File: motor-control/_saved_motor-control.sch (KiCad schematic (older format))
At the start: 8 parts

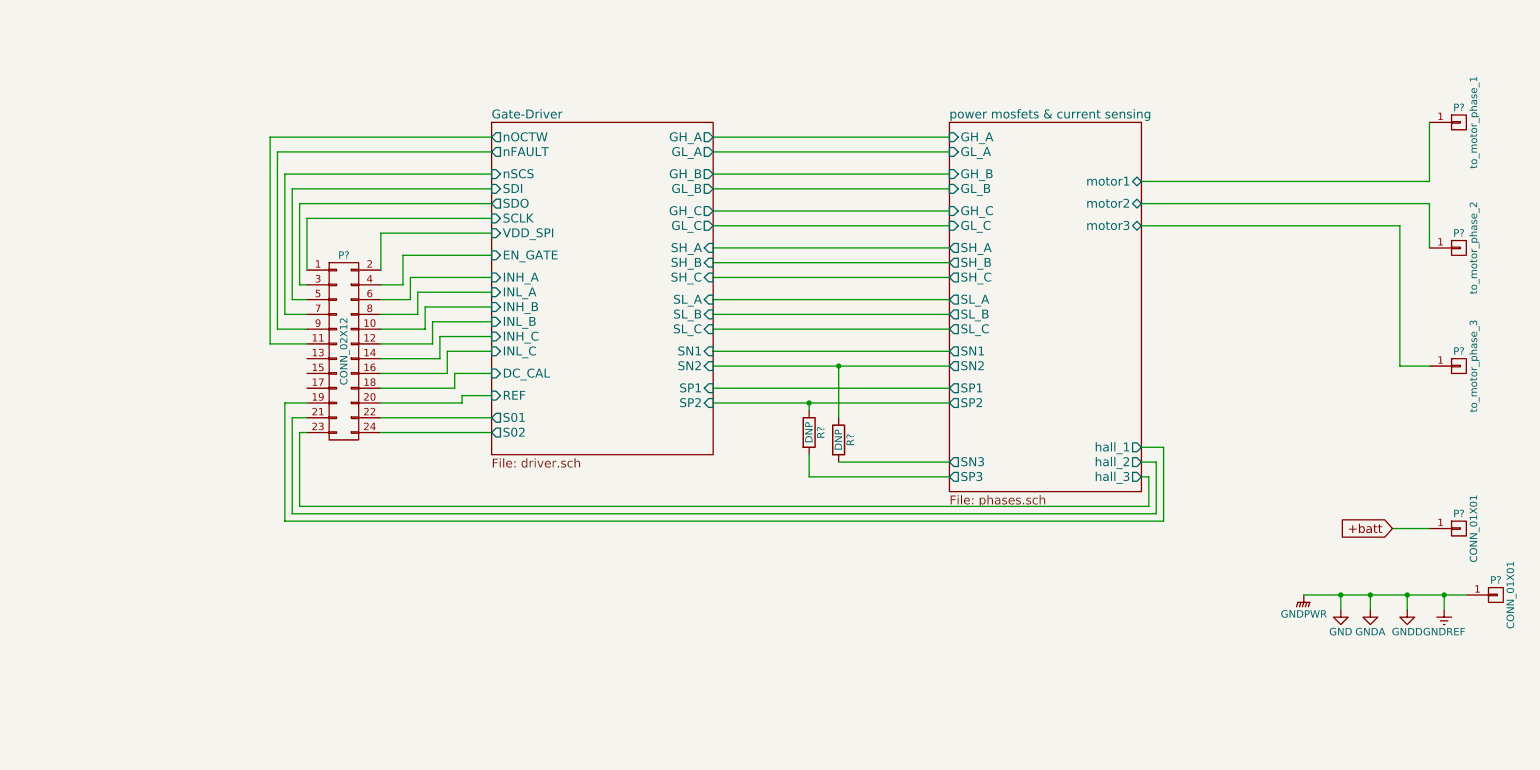
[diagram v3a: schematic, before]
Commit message: Annotated schematic & matched footprints
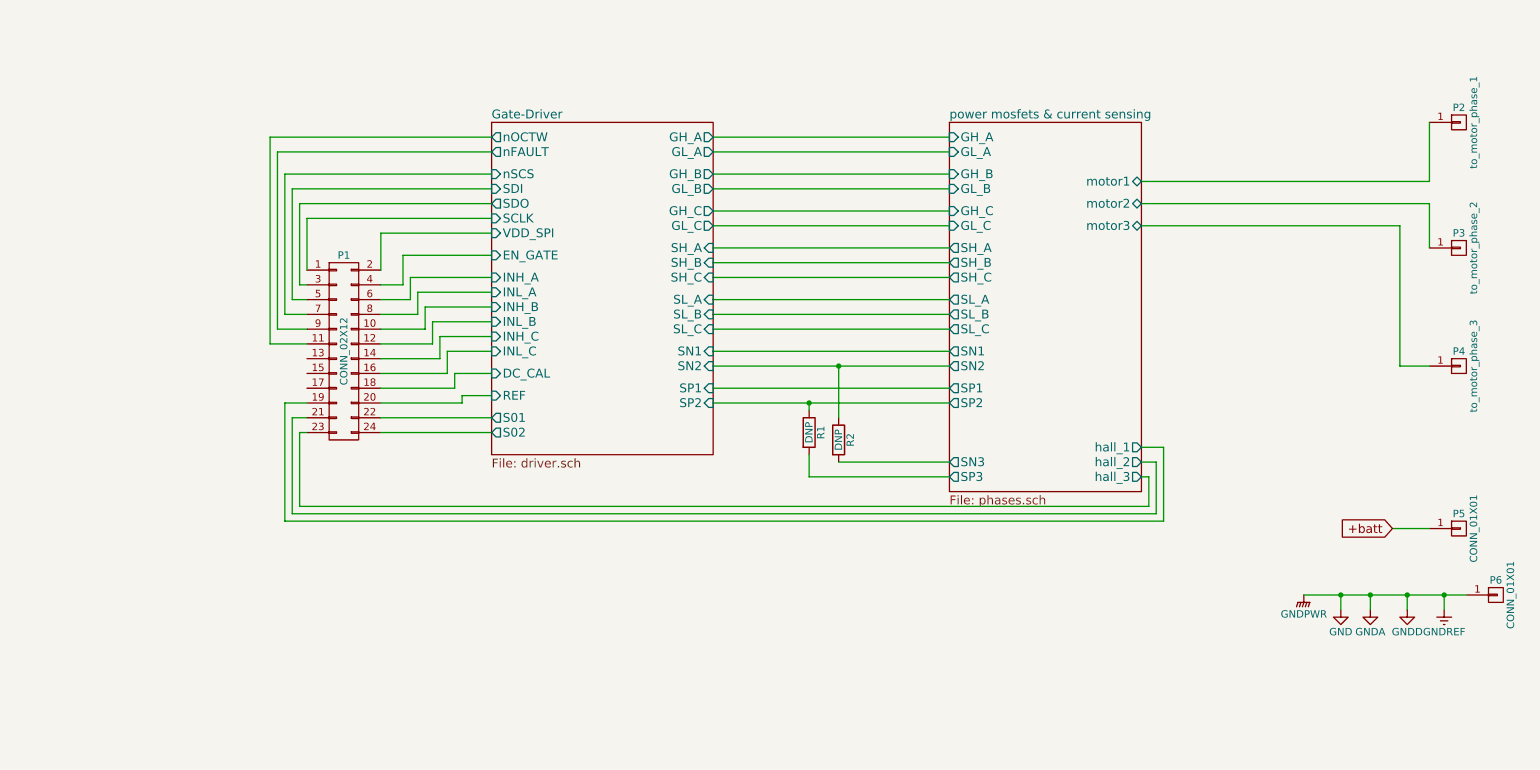
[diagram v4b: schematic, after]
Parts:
- P1: renamed from P?; footprint (none) -> Pin_Headers:Pin_Header_Straight_2x12
- P2, P3, P4, P5, P6: renamed from P?; footprint (none) -> Pin_Headers:Pin_Header_Straight_1x01
- R1, R2: renamed from R?; footprint (none) -> Resistors_SMD:R_0805
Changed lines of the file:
@@
 $EndSheet
 $Comp
-L CONN_01X01 P?
+L CONN_01X01 P2
 U 1 1 5643889D
 P 10750 2150
-F 0 "P?" H 10750 2250 50  0000 C CNN
+F 0 "P2" H 10750 2250 50  0000 C CNN
 F 1 "to_motor_phase_1" V 10850 2150 50  0000 C CNN
-F 2 "" H 10750 2150 60  0000 C CNN
+F 2 "Pin_Headers:Pin_Header_Straight_1x01" H 10750 2150 60  0001 C CNN
 F 3 "" H 10750 2150 60  0000 C CNN
 	1    10750 2150
@@
 $EndComp
 $Comp
-L CONN_01X01 P?
+L CONN_01X01 P3
 U 1 1 56438B24
 P 10750 3000
-F 0 "P?" H 10750 3100 50  0000 C CNN
+F 0 "P3" H 10750 3100 50  0000 C CNN
 F 1 "to_motor_phase_2" V 10850 3000 50  0000 C CNN
-F 2 "" H 10750 3000 60  0000 C CNN
+F 2 "Pin_Headers:Pin_Header_Straight_1x01" H 10750 3000 60  0001 C CNN
 F 3 "" H 10750 3000 60  0000 C CNN
 	1    10750 3000
@@
 $EndComp
 $Comp
-L CONN_01X01 P?
+L CONN_01X01 P4
 U 1 1 56438C23
 P 10750 3800
-F 0 "P?" H 10750 3900 50  0000 C CNN
+F 0 "P4" H 10750 3900 50  0000 C CNN
 F 1 "to_motor_phase_3" V 10850 3800 50  0000 C CNN
-F 2 "" H 10750 3800 60  0000 C CNN
+F 2 "Pin_Headers:Pin_Header_Straight_1x01" H 10750 3800 60  0001 C CNN
 F 3 "" H 10750 3800 60  0000 C CNN
 	1    10750 3800
@@
 +batt
 $Comp
-L CONN_02X12 P?
+L CONN_02X12 P1
 U 1 1 5653585A
 P 3200 3700
-F 0 "P?" H 3200 4350 50  0000 C CNN
+F 0 "P1" H 3200 4350 50  0000 C CNN
 F 1 "CONN_02X12" V 3200 3700 50  0000 C CNN
-F 2 "" H 3200 2500 60  0000 C CNN
+F 2 "Pin_Headers:Pin_Header_Straight_2x12" H 3200 2500 60  0001 C CNN
 F 3 "" H 3200 2500 60  0000 C CNN
 	1    3200 3700
@@
 $EndComp
 $Comp
-L R R?
+L R R1
 U 1 1 56555BF6
 P 6350 4250
-F 0 "R?" V 6430 4250 50  0000 C CNN
+F 0 "R1" V 6430 4250 50  0000 C CNN
 F 1 "DNP" V 6350 4250 50  0000 C CNN
-F 2 "" V 6280 4250 30  0000 C CNN
+F 2 "Resistors_SMD:R_0805" V 6280 4250 30  0001 C CNN
 F 3 "" H 6350 4250 30  0000 C CNN
 	1    6350 4250
@@
 $EndComp
 $Comp
-L R R?
+L R R2
 U 1 1 56555DC0
 P 6550 4300
-F 0 "R?" V 6630 4300 50  0000 C CNN
+F 0 "R2" V 6630 4300 50  0000 C CNN
 F 1 "DNP" V 6550 4300 50  0000 C CNN
-F 2 "" V 6480 4300 30  0000 C CNN
+F 2 "Resistors_SMD:R_0805" V 6480 4300 30  0001 C CNN
 F 3 "" H 6550 4300 30  0000 C CNN
 	1    6550 4300
@@
 	2800 4050 2950 4050
 $Comp
-L CONN_01X01 P?
+L CONN_01X01 P5
 U 1 1 5656A75D
 P 10750 4900
-F 0 "P?" H 10750 5000 50  0000 C CNN
+F 0 "P5" H 10750 5000 50  0000 C CNN
 F 1 "CONN_01X01" V 10850 4900 50  0000 C CNN
-F 2 "" H 10750 4900 60  0000 C CNN
+F 2 "Pin_Headers:Pin_Header_Straight_1x01" H 10750 4900 60  0001 C CNN
 F 3 "" H 10750 4900 60  0000 C CNN
 	1    10750 4900
@@
 	10550 4900 10300 4900
 $Comp
-L GND #PWR?
+L GND #PWR01
 U 1 1 5656AFE6
 P 9950 5450
-F 0 "#PWR?" H 9950 5200 50  0001 C CNN
+F 0 "#PWR01" H 9950 5200 50  0001 C CNN
 F 1 "GND" H 9950 5300 50  0000 C CNN
 F 2 "" H 9950 5450 60  0000 C CNN
@@
 $EndComp
 $Comp
-L GNDA #PWR?
+L GNDA #PWR02
 U 1 1 5656B164
 P 10150 5450
-F 0 "#PWR?" H 10150 5200 50  0001 C CNN
+F 0 "#PWR02" H 10150 5200 50  0001 C CNN
 F 1 "GNDA" H 10150 5300 50  0000 C CNN
 F 2 "" H 10150 5450 60  0000 C CNN
@@
 $EndComp
 $Comp
-L GNDD #PWR?
+L GNDD #PWR03
 U 1 1 5656B2E2
 P 10400 5450
-F 0 "#PWR?" H 10400 5200 50  0001 C CNN
+F 0 "#PWR03" H 10400 5200 50  0001 C CNN
 F 1 "GNDD" H 10400 5300 50  0000 C CNN
 F 2 "" H 10400 5450 60  0000 C CNN
@@
 $EndComp
 $Comp
-L GNDPWR #PWR?
+L GNDPWR #PWR04
 U 1 1 5656B460
 P 9700 5350
-F 0 "#PWR?" H 9700 5150 50  0001 C CNN
+F 0 "#PWR04" H 9700 5150 50  0001 C CNN
 F 1 "GNDPWR" H 9700 5220 50  0000 C CNN
 F 2 "" H 9700 5300 60  0000 C CNN
@@
 $EndComp
 $Comp
-L GNDREF #PWR?
+L GNDREF #PWR05
 U 1 1 5656B5DE
 P 10650 5450
-F 0 "#PWR?" H 10650 5200 50  0001 C CNN
+F 0 "#PWR05" H 10650 5200 50  0001 C CNN
 F 1 "GNDREF" H 10650 5300 50  0000 C CNN
 F 2 "" H 10650 5450 60  0000 C CNN
@@
 $EndComp
 $Comp
-L CONN_01X01 P?
+L CONN_01X01 P6
 U 1 1 5656B761
 P 11000 5350
-F 0 "P?" H 11000 5450 50  0000 C CNN
+F 0 "P6" H 11000 5450 50  0000 C CNN
 F 1 "CONN_01X01" V 11100 5350 50  0000 C CNN
-F 2 "" H 11000 5350 60  0000 C CNN
+F 2 "Pin_Headers:Pin_Header_Straight_1x01" H 11000 5350 60  0001 C CNN
 F 3 "" H 11000 5350 60  0000 C CNN
 	1    11000 5350

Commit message: Significant board changes, fixed hall ftpnt
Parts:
- P2, P3, P4: footprint Pin_Headers:Pin_Header_Straight_1x01 -> Connect:Banana_Jack_1Pin
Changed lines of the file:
@@
 F 0 "P2" H 10750 2250 50  0000 C CNN
 F 1 "to_motor_phase_1" V 10850 2150 50  0000 C CNN
-F 2 "Pin_Headers:Pin_Header_Straight_1x01" H 10750 2150 60  0001 C CNN
+F 2 "Connect:Banana_Jack_1Pin" H 10750 2150 60  0001 C CNN
 F 3 "" H 10750 2150 60  0000 C CNN
 	1    10750 2150
@@
 F 0 "P3" H 10750 3100 50  0000 C CNN
 F 1 "to_motor_phase_2" V 10850 3000 50  0000 C CNN
-F 2 "Pin_Headers:Pin_Header_Straight_1x01" H 10750 3000 60  0001 C CNN
+F 2 "Connect:Banana_Jack_1Pin" H 10750 3000 60  0001 C CNN
 F 3 "" H 10750 3000 60  0000 C CNN
 	1    10750 3000
@@
 F 0 "P4" H 10750 3900 50  0000 C CNN
 F 1 "to_motor_phase_3" V 10850 3800 50  0000 C CNN
-F 2 "Pin_Headers:Pin_Header_Straight_1x01" H 10750 3800 60  0001 C CNN
+F 2 "Connect:Banana_Jack_1Pin" H 10750 3800 60  0001 C CNN
 F 3 "" H 10750 3800 60  0000 C CNN
 	1    10750 3800

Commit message: Just trying to get things together
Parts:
- P5, P6: footprint Pin_Headers:Pin_Header_Straight_1x01 -> Connect:Banana_Jack_1Pin
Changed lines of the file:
@@
 F 0 "P5" H 10750 5000 50  0000 C CNN
 F 1 "CONN_01X01" V 10850 4900 50  0000 C CNN
-F 2 "Pin_Headers:Pin_Header_Straight_1x01" H 10750 4900 60  0001 C CNN
+F 2 "Connect:Banana_Jack_1Pin" H 10750 4900 60  0001 C CNN
 F 3 "" H 10750 4900 60  0000 C CNN
 	1    10750 4900
@@
 F 0 "P6" H 11000 5450 50  0000 C CNN
 F 1 "CONN_01X01" V 11100 5350 50  0000 C CNN
-F 2 "Pin_Headers:Pin_Header_Straight_1x01" H 11000 5350 60  0001 C CNN
+F 2 "Connect:Banana_Jack_1Pin" H 11000 5350 60  0001 C CNN
 F 3 "" H 11000 5350 60  0000 C CNN
 	1    11000 5350

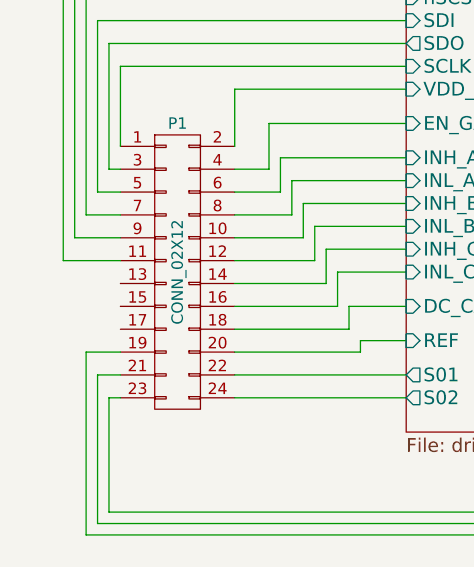
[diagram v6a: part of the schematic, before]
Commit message: Added VCC in shematic
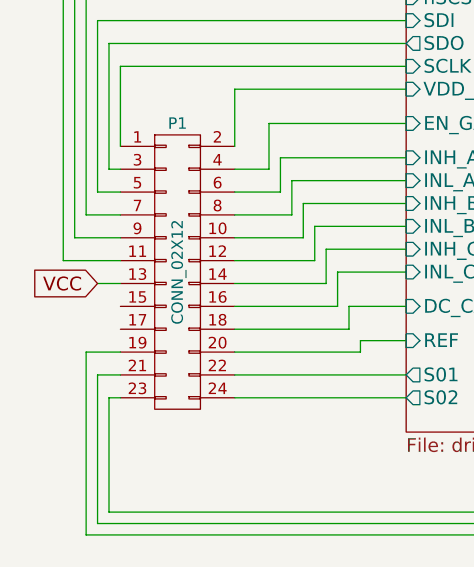
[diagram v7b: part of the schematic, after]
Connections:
- net VCC: now reaches P1.13 (P13)
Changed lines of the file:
@@
 	10650 5450 10650 5350
 Connection ~ 10650 5350
+Text GLabel 2850 3750 0    60   Input ~ 0
+VCC
+Wire Wire Line
+	2850 3750 2950 3750
 $EndSCHEMATC

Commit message: Added temp sensor ADT7301 sot-23
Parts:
- added P7: CONN_01X04, Pin_Headers:Pin_Header_Straight_1x04, symbol CONN_01X04
- added U5: ADT7301, p16261:ADT7301, symbol ADT7301
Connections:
- net GND: now also U5.1 (GND)
- net VCC: now also U5.3 (Vdd)
- new net: P7.4 (P4), U5.2 (DIN)
- new net: P7.3 (P3), U5.4 (SCLK)
- new net: P7.2 (P2), U5.5 (~CS)
- new net: P7.1 (P1), U5.6 (DOUT)
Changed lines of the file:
@@
 	10550 4900 10300 4900
 $Comp
-L GND #PWR01
+L GND #PWR3
 U 1 1 5656AFE6
 P 9950 5450
-F 0 "#PWR01" H 9950 5200 50  0001 C CNN
+F 0 "#PWR3" H 9950 5200 50  0001 C CNN
 F 1 "GND" H 9950 5300 50  0000 C CNN
 F 2 "" H 9950 5450 60  0000 C CNN
@@
 $EndComp
 $Comp
-L GNDA #PWR02
+L GNDA #PWR4
 U 1 1 5656B164
 P 10150 5450
-F 0 "#PWR02" H 10150 5200 50  0001 C CNN
+F 0 "#PWR4" H 10150 5200 50  0001 C CNN
 F 1 "GNDA" H 10150 5300 50  0000 C CNN
 F 2 "" H 10150 5450 60  0000 C CNN
@@
 $EndComp
 $Comp
-L GNDD #PWR03
+L GNDD #PWR5
 U 1 1 5656B2E2
 P 10400 5450
-F 0 "#PWR03" H 10400 5200 50  0001 C CNN
+F 0 "#PWR5" H 10400 5200 50  0001 C CNN
 F 1 "GNDD" H 10400 5300 50  0000 C CNN
 F 2 "" H 10400 5450 60  0000 C CNN
@@
 $EndComp
 $Comp
-L GNDPWR #PWR04
+L GNDPWR #PWR2
 U 1 1 5656B460
 P 9700 5350
-F 0 "#PWR04" H 9700 5150 50  0001 C CNN
+F 0 "#PWR2" H 9700 5150 50  0001 C CNN
 F 1 "GNDPWR" H 9700 5220 50  0000 C CNN
 F 2 "" H 9700 5300 60  0000 C CNN
@@
 $EndComp
 $Comp
-L GNDREF #PWR05
+L GNDREF #PWR6
 U 1 1 5656B5DE
 P 10650 5450
-F 0 "#PWR05" H 10650 5200 50  0001 C CNN
+F 0 "#PWR6" H 10650 5200 50  0001 C CNN
 F 1 "GNDREF" H 10650 5300 50  0000 C CNN
 F 2 "" H 10650 5450 60  0000 C CNN
@@
 Wire Wire Line
 	2850 3750 2950 3750
+$Comp
+L ADT7301 U5
+U 1 1 568CE9F4
+P 5800 5600
+F 0 "U5" H 5750 5850 60  0000 C CNN
+F 1 "ADT7301" H 5800 5450 60  0000 C CNN
+F 2 "p16261:ADT7301" H 5550 5950 60  0001 C CNN
+F 3 "" H 5550 5950 60  0000 C CNN
+	1    5800 5600
+	1    0    0    -1
+$EndComp
+$Comp
+L CONN_01X04 P7
+U 1 1 568CF198
+P 5750 6300
+F 0 "P7" H 5750 6550 50  0000 C CNN
+F 1 "CONN_01X04" V 5850 6300 50  0000 C CNN
+F 2 "Pin_Headers:Pin_Header_Straight_1x04" H 5750 6300 50  0001 C CNN
+F 3 "" H 5750 6300 50  0000 C CNN
+	1    5750 6300
+	0    1    1    0
+$EndComp
+Wire Wire Line
+	6200 5650 6200 6000
+Wire Wire Line
+	6200 6000 5700 6000
+Wire Wire Line
+	5700 6000 5700 6100
+Wire Wire Line
+	6200 5550 6250 5550
+Wire Wire Line
+	6250 5550 6250 6050
+Wire Wire Line
+	6250 6050 5800 6050
+Wire Wire Line
+	5800 6050 5800 6100
+Wire Wire Line
+	6200 5450 6300 5450
+Wire Wire Line
+	6300 5450 6300 6100
+Wire Wire Line
+	6300 6100 5900 6100
+Wire Wire Line
+	5250 6100 5600 6100
+Text GLabel 5050 5650 0    60   Input ~ 0
+VCC
+Wire Wire Line
+	5250 6100 5250 5550
+Wire Wire Line
+	5250 5550 5350 5550
+Wire Wire Line
+	5050 5650 5350 5650
+$Comp
+L GND #PWR1
+U 1 1 568D1B96
+P 5150 5450
+F 0 "#PWR1" H 5150 5200 50  0001 C CNN
+F 1 "GND" H 5150 5300 50  0000 C CNN
+F 2 "" H 5150 5450 60  0000 C CNN
+F 3 "" H 5150 5450 60  0000 C CNN
+	1    5150 5450
+	0    1    1    0
+$EndComp
+Wire Wire Line
+	5150 5450 5350 5450
 $EndSCHEMATC
